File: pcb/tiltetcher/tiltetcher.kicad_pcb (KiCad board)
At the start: 2 copper layers, 9 parts, among them J1 Peltier_Terminal, J2 12V_Terminal, J3 Sensor_Terminal, Q1 IRF640

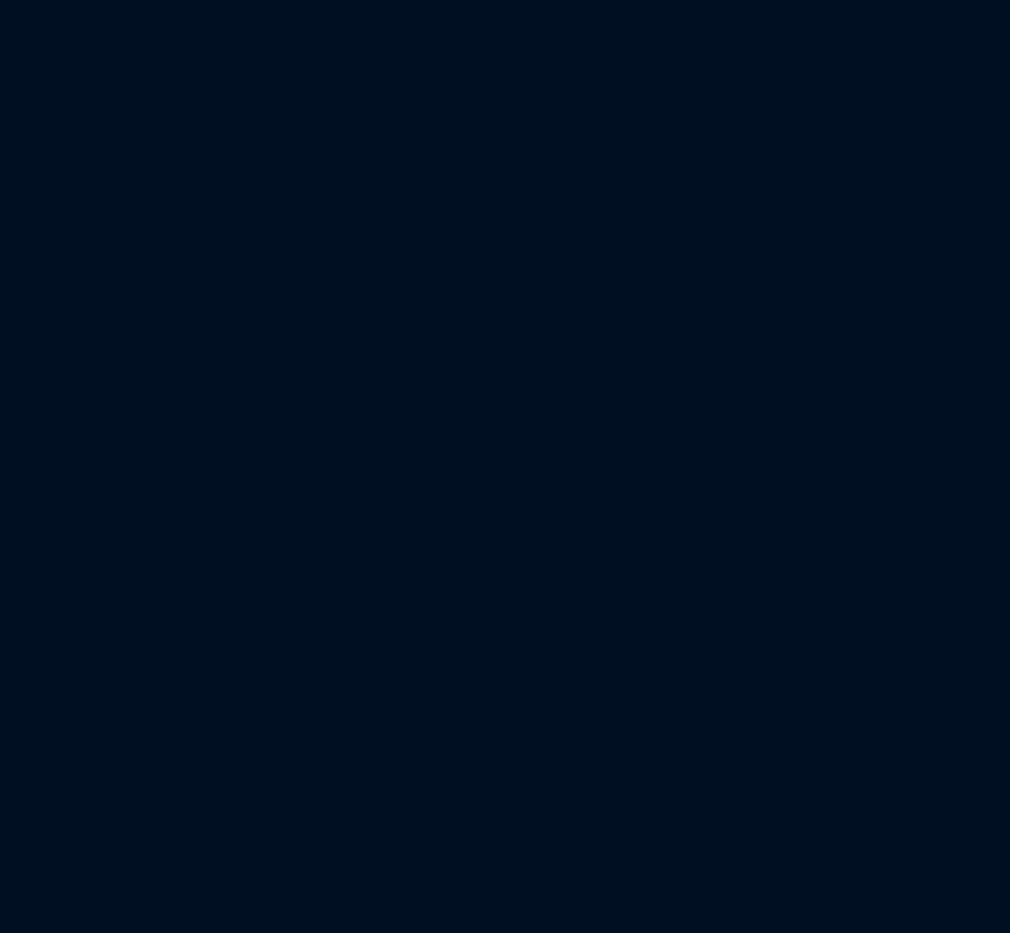
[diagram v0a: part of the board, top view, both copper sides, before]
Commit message: gpios are now switching correctly
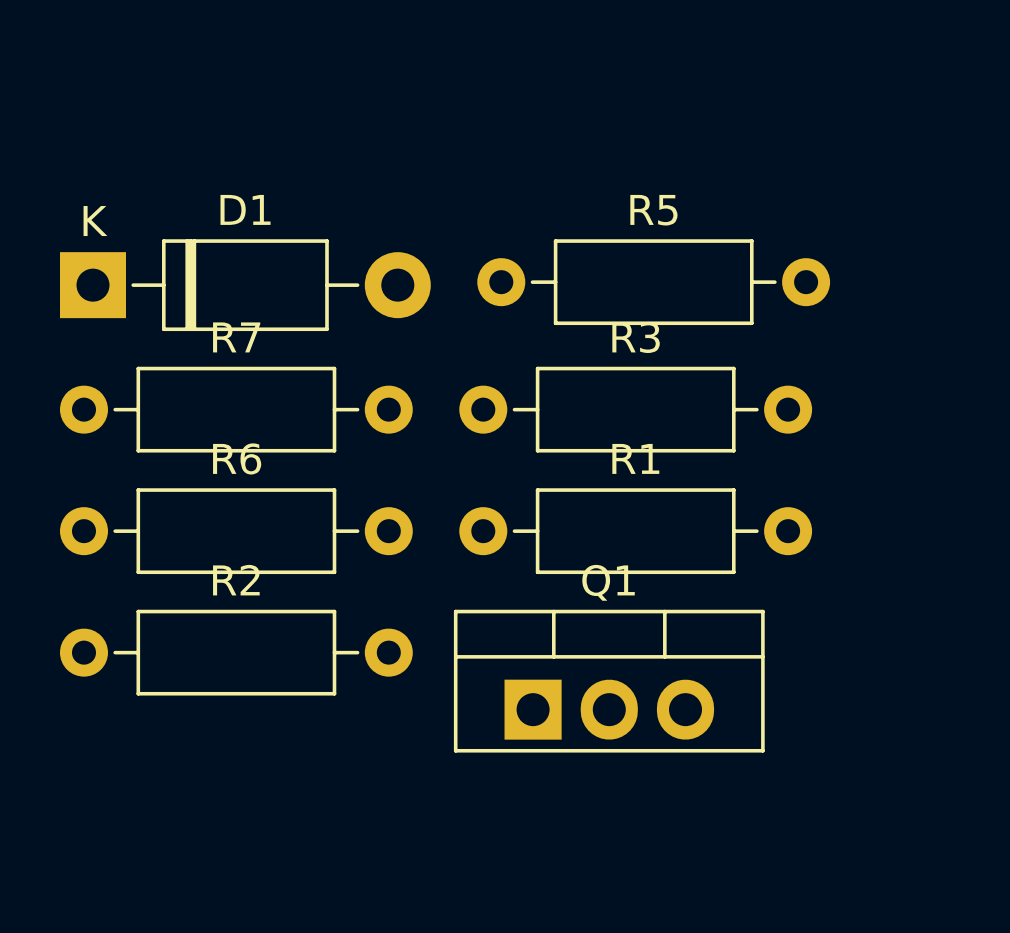
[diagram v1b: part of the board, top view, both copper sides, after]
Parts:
- added D1: 1N4001, Diode_THT:D_DO-41_SOD81_P10.16mm_Horizontal, F.Cu at (40.6, 43.2)
- added Q1: IRF3205, Package_TO_SOT_THT:TO-220-3_Vertical, F.Cu at (55.3, 57.3)
- added R1: 3k, Resistor_THT:R_Axial_DIN0207_L6.3mm_D2.5mm_P10.16mm_Horizontal, F.Cu at (53.6, 51.4)
- added R2: 1k, Resistor_THT:R_Axial_DIN0207_L6.3mm_D2.5mm_P10.16mm_Horizontal, F.Cu at (40.3, 55.4)
- added R3: 1k, Resistor_THT:R_Axial_DIN0207_L6.3mm_D2.5mm_P10.16mm_Horizontal, F.Cu at (53.6, 47.3)
- added R5: R220, Resistor_THT:R_Axial_DIN0207_L6.3mm_D2.5mm_P10.16mm_Horizontal, F.Cu at (54.2, 43.1)
- added R6: R220, Resistor_THT:R_Axial_DIN0207_L6.3mm_D2.5mm_P10.16mm_Horizontal, F.Cu at (40.3, 51.4)
- added R7: R220, Resistor_THT:R_Axial_DIN0207_L6.3mm_D2.5mm_P10.16mm_Horizontal, F.Cu at (40.3, 47.3)
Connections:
- A1 pad 15: unconnected-(A1-Pad15) -> /LED_MAIN_PWR
- A1 pad 16: unconnected-(A1-Pad16) -> /LED_HTR_WRN
- A1 pad 17: unconnected-(A1-Pad17) -> /LED_HTR_RDY
